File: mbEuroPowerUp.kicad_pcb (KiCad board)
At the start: 2 copper layers, 60 x 21.1 mm, 10 parts, among them J1 Conn_02x08_Odd_Even, J2 USB_B_Micro, J3 Conn_01x03, J4 Conn_02x02_Odd_Even, J5 Conn_01x02, J6 Conn_01x02

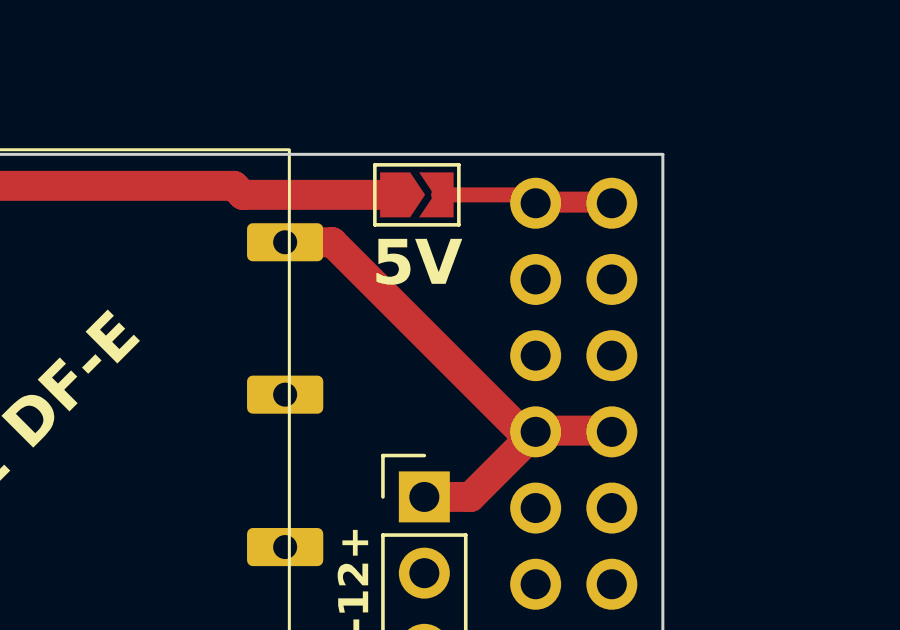
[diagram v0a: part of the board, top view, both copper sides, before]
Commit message: Fix 5V Pins
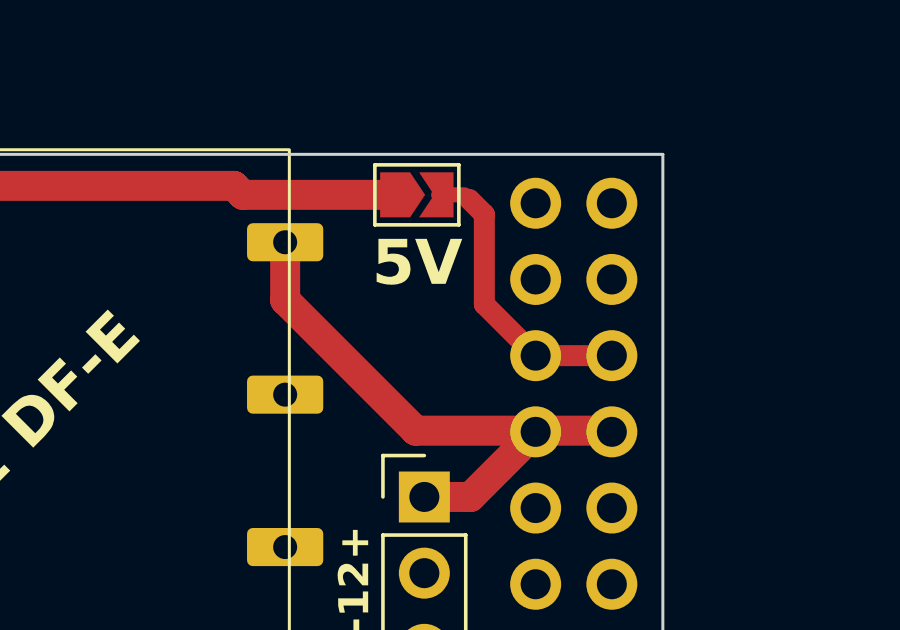
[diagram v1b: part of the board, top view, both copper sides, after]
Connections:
- J1 pad 11: unconnected-(J1-Pin_11-Pad11) -> Net-(J1-Pin_11)
- J1 pad 12: unconnected-(J1-Pin_12-Pad12) -> Net-(J1-Pin_11)
- J1 pad 15: Net-(J1-Pin_15) -> unconnected-(J1-Pin_15-Pad15)
- J1 pad 16: Net-(J1-Pin_15) -> unconnected-(J1-Pin_16-Pad16)
- JP1 pad 2: Net-(J1-Pin_15) -> Net-(J1-Pin_11)
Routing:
- net Net-(J1-Pin_11): track 0.00 -> 9.75 mm
- net Net-(J1-Pin_15): track 5.97 -> 0.00 mm
- net +12V: track 18.2 -> 19.3 mm
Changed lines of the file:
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@@
 	(net 0 "")
 	(net 1 "unconnected-(U1-TRM-Pad6)")
-	(net 2 "Net-(J1-Pin_15)")
+	(net 2 "Net-(J1-Pin_11)")
 	(net 3 "GND")
 	(net 4 "unconnected-(J1-Pin_14-Pad14)")
 	(net 5 "-12V")
-	(net 6 "unconnected-(J1-Pin_11-Pad11)")
+	(net 6 "unconnected-(J1-Pin_16-Pad16)")
 	(net 7 "Net-(D1-A)")
 	(net 8 "+12V")
 	(net 9 "Net-(D2-A)")
-	(net 10 "unconnected-(J1-Pin_12-Pad12)")
+	(net 10 "unconnected-(J1-Pin_15-Pad15)")
 	(net 11 "unconnected-(J1-Pin_13-Pad13)")
 	(net 12 "+5V")
@@
 			(size 0.3 0.3)
 			(layers "F.Cu" "F.Mask")
-			(net 2 "Net-(J1-Pin_15)")
+			(net 2 "Net-(J1-Pin_11)")
 			(pinfunction "B")
 			(pintype "passive")
@@
 			(layers "*.Cu" "*.Mask")
 			(remove_unused_layers no)
-			(net 6 "unconnected-(J1-Pin_11-Pad11)")
+			(net 2 "Net-(J1-Pin_11)")
 			(pinfunction "Pin_11")
 			(pintype "passive")
@@
 			(layers "*.Cu" "*.Mask")
 			(remove_unused_layers no)
-			(net 10 "unconnected-(J1-Pin_12-Pad12)")
+			(net 2 "Net-(J1-Pin_11)")
 			(pinfunction "Pin_12")
 			(pintype "passive")
@@
 			(layers "*.Cu" "*.Mask")
 			(remove_unused_layers no)
-			(net 2 "Net-(J1-Pin_15)")
+			(net 10 "unconnected-(J1-Pin_15-Pad15)")
 			(pinfunction "Pin_15")
 			(pintype "passive")
@@
 			(layers "*.Cu" "*.Mask")
 			(remove_unused_layers no)
-			(net 2 "Net-(J1-Pin_15)")
+			(net 6 "unconnected-(J1-Pin_16-Pad16)")
 			(pinfunction "Pin_16")
 			(pintype "passive")
@@
 	)
 	(segment
-		(start 165.6 78.84)
-		(end 163.06 78.84)
-		(width 0.7)
-		(layer "F.Cu")
-		(net 2)
-	)
-	(segment
-		(start 162.82 78.6)
-		(end 163.06 78.84)
+		(start 161.25 79.25)
+		(end 160.75 78.75)
 		(width 0.7)
 		(layer "F.Cu")
@@
 	(segment
 		(start 159.725 78.6)
-		(end 162.82 78.6)
+		(end 160.6 78.6)
 		(width 0.5)
+		(layer "F.Cu")
+		(net 2)
+	)
+	(segment
+		(start 162.96 83.96)
+		(end 161.25 82.25)
+		(width 0.7)
+		(layer "F.Cu")
+		(net 2)
+	)
+	(segment
+		(start 161.25 82.25)
+		(end 161.25 79.25)
+		(width 0.7)
+		(layer "F.Cu")
+		(net 2)
+	)
+	(segment
+		(start 165.5 83.96)
+		(end 162.96 83.96)
+		(width 0.7)
+		(layer "F.Cu")
+		(net 2)
+	)
+	(segment
+		(start 160.6 78.6)
+		(end 160.75 78.75)
+		(width 0.2)
 		(layer "F.Cu")
 		(net 2)
@@
 	)
 	(segment
+		(start 154.61 82.11)
+		(end 154.61 80.18)
+		(width 1)
+		(layer "F.Cu")
+		(net 8)
+	)
+	(segment
+		(start 158.96 86.46)
+		(end 154.61 82.11)
+		(width 1)
+		(layer "F.Cu")
+		(net 8)
+	)
+	(segment
 		(start 165.6 86.46)
-		(end 162.46 86.46)
-		(width 1)
-		(layer "F.Cu")
-		(net 8)
-	)
-	(segment
-		(start 162.46 86.46)
-		(end 156.18 80.18)
+		(end 158.96 86.46)
 		(width 1)
 		(layer "F.Cu")
@@
 		(width 1)
 		(layer "F.Cu")
-		(net 8)
-	)
-	(segment
-		(start 156.18 80.18)
-		(end 154.61 80.18)
-		(width 1)
-		(layer "F.Cu")
